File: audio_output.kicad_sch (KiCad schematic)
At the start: 33 parts, among them J8 NCJ6FA-H-0, J9 NCJ6FA-H-0, U5 OPA1656ID, U6 THAT1646, U7 THAT1646

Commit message: TVS fix
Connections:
- net AUDIO_OUT_R: now also R20.2
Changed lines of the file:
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@@
 	(wire
 		(pts
-			(xy 60.96 119.38) (xy 64.77 119.38)
-		)
-		(stroke
-			(width 0)
-			(type default)
-		)
-	)
-	(wire
-		(pts
-			(xy 99.06 166.37) (xy 99.06 168.91)
+			(xy 99.06 161.29) (xy 99.06 168.91)
 		)
 		(stroke
@@
 	(wire
 		(pts
-			(xy 81.28 191.77) (xy 81.28 179.07)
+			(xy 81.28 195.58) (xy 81.28 179.07)
 		)
 		(stroke
@@
 	(wire
 		(pts
-			(xy 135.89 166.37) (xy 135.89 168.91)
+			(xy 135.89 161.29) (xy 135.89 168.91)
 		)
 		(stroke
@@
 	(wire
 		(pts
-			(xy 99.06 189.23) (xy 99.06 191.77)
+			(xy 99.06 189.23) (xy 99.06 195.58)
 		)
 		(stroke
@@
 	(wire
 		(pts
-			(xy 118.11 191.77) (xy 118.11 179.07)
+			(xy 118.11 195.58) (xy 118.11 179.07)
 		)
 		(stroke
@@
 	(wire
 		(pts
-			(xy 135.89 189.23) (xy 135.89 191.77)
+			(xy 135.89 189.23) (xy 135.89 195.58)
 		)
 		(stroke
@@
 	(wire
 		(pts
+			(xy 59.69 119.38) (xy 64.77 119.38)
+		)
+		(stroke
+			(width 0)
+			(type default)
+		)
+	)
+	(wire
+		(pts
 			(xy 147.32 55.88) (xy 156.21 55.88)
 		)
@@
 	(symbol
 		(lib_id "power:+12VA")
-		(at 99.06 166.37 0)
+		(at 99.06 161.29 0)
 		(unit 1)
 		(exclude_from_sim no)
@@
 		(fields_autoplaced yes)
 		(property "Reference" "#PWR036"
-			(at 99.06 170.18 0)
+			(at 99.06 165.1 0)
 			(effects
 				(font
@@
 		)
 		(property "Value" "+12VA"
-			(at 99.06 161.29 0)
+			(at 99.06 156.21 0)
 			(effects
 				(font
@@
 		)
 		(property "Footprint" ""
-			(at 99.06 166.37 0)
+			(at 99.06 161.29 0)
 			(effects
 				(font
@@
 		)
 		(property "Datasheet" ""
-			(at 99.06 166.37 0)
+			(at 99.06 161.29 0)
 			(effects
 				(font
@@
 		)
 		(property "Description" "Power symbol creates a global label with name \"+12VA\""
-			(at 99.06 166.37 0)
+			(at 99.06 161.29 0)
 			(effects
 				(font
@@
 	(symbol
 		(lib_id "power:-12VA")
-		(at 99.06 191.77 180)
+		(at 99.06 195.58 180)
 		(unit 1)
 		(exclude_from_sim no)
@@
 		(fields_autoplaced yes)
 		(property "Reference" "#PWR037"
-			(at 99.06 187.96 0)
+			(at 99.06 191.77 0)
 			(effects
 				(font
@@
 		)
 		(property "Value" "-12VA"
-			(at 99.06 196.85 0)
+			(at 99.06 200.66 0)
 			(effects
 				(font
@@
 		)
 		(property "Footprint" ""
-			(at 99.06 191.77 0)
+			(at 99.06 195.58 0)
 			(effects
 				(font
@@
 		)
 		(property "Datasheet" ""
-			(at 99.06 191.77 0)
+			(at 99.06 195.58 0)
 			(effects
 				(font
@@
 		)
 		(property "Description" "Power symbol creates a global label with name \"-12VA\""
-			(at 99.06 191.77 0)
+			(at 99.06 195.58 0)
 			(effects
 				(font
@@
 	(symbol
 		(lib_id "power:-12VA")
-		(at 135.89 191.77 180)
+		(at 135.89 195.58 180)
 		(unit 1)
 		(exclude_from_sim no)
@@
 		(fields_autoplaced yes)
 		(property "Reference" "#PWR040"
-			(at 135.89 187.96 0)
+			(at 135.89 191.77 0)
 			(effects
 				(font
@@
 		)
 		(property "Value" "-12VA"
-			(at 135.89 196.85 0)
+			(at 135.89 200.66 0)
 			(effects
 				(font
@@
 		)
 		(property "Footprint" ""
-			(at 135.89 191.77 0)
+			(at 135.89 195.58 0)
 			(effects
 				(font
@@
 		)
 		(property "Datasheet" ""
-			(at 135.89 191.77 0)
+			(at 135.89 195.58 0)
 			(effects
 				(font
@@
 		)
 		(property "Description" "Power symbol creates a global label with name \"-12VA\""
-			(at 135.89 191.77 0)
+			(at 135.89 195.58 0)
 			(effects
 				(font
@@
 	(symbol
 		(lib_id "power:GND")
-		(at 81.28 191.77 0)
+		(at 81.28 195.58 0)
 		(unit 1)
 		(exclude_from_sim no)
@@
 		(fields_autoplaced yes)
 		(property "Reference" "#PWR035"
-			(at 81.28 198.12 0)
+			(at 81.28 201.93 0)
 			(effects
 				(font
@@
 		)
 		(property "Value" "GND"
-			(at 81.28 196.85 0)
+			(at 81.28 200.66 0)
 			(effects
 				(font
@@
 		)
 		(property "Footprint" ""
-			(at 81.28 191.77 0)
+			(at 81.28 195.58 0)
 			(effects
 				(font
@@
 		)
 		(property "Datasheet" ""
-			(at 81.28 191.77 0)
+			(at 81.28 195.58 0)
 			(effects
 				(font
@@
 		)
 		(property "Description" "Power symbol creates a global label with name \"GND\" , ground"
-			(at 81.28 191.77 0)
+			(at 81.28 195.58 0)
 			(effects
 				(font
@@
 	(symbol
 		(lib_id "power:+12VA")
-		(at 135.89 166.37 0)
+		(at 135.89 161.29 0)
 		(unit 1)
 		(exclude_from_sim no)
@@
 		(fields_autoplaced yes)
 		(property "Reference" "#PWR039"
-			(at 135.89 170.18 0)
+			(at 135.89 165.1 0)
 			(effects
 				(font
@@
 		)
 		(property "Value" "+12VA"
-			(at 135.89 161.29 0)
+			(at 135.89 156.21 0)
 			(effects
 				(font
@@
 		)
 		(property "Footprint" ""
-			(at 135.89 166.37 0)
+			(at 135.89 161.29 0)
 			(effects
 				(font
@@
 		)
 		(property "Datasheet" ""
-			(at 135.89 166.37 0)
+			(at 135.89 161.29 0)
 			(effects
 				(font
@@
 		)
 		(property "Description" "Power symbol creates a global label with name \"+12VA\""
-			(at 135.89 166.37 0)
+			(at 135.89 161.29 0)
 			(effects
 				(font
@@
 	(symbol
 		(lib_id "power:GND")
-		(at 118.11 191.77 0)
+		(at 118.11 195.58 0)
 		(unit 1)
 		(exclude_from_sim no)
@@
 		(fields_autoplaced yes)
 		(property "Reference" "#PWR038"
-			(at 118.11 198.12 0)
+			(at 118.11 201.93 0)
 			(effects
 				(font
@@
 		)
 		(property "Value" "GND"
-			(at 118.11 196.85 0)
+			(at 118.11 200.66 0)
 			(effects
 				(font
@@
 		)
 		(property "Footprint" ""
-			(at 118.11 191.77 0)
+			(at 118.11 195.58 0)
 			(effects
 				(font
@@
 		)
 		(property "Datasheet" ""
-			(at 118.11 191.77 0)
+			(at 118.11 195.58 0)
 			(effects
 				(font
@@
 		)
 		(property "Description" "Power symbol creates a global label with name \"GND\" , ground"
-			(at 118.11 191.77 0)
+			(at 118.11 195.58 0)
 			(effects
 				(font

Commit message: working on output
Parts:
- C16, C17: value C -> 100p C0G
- R19, R20: value R -> 2k2 1%
- R21, R22: value R -> 15k
- RV1, RV2: value R_Potentiometer_Trim -> 10k
- renumbered D8 to D10, D9 to D11, D10 to D12, D3 to D5, D4 to D6, D5 to D7, D6 to D8, D7 to D9
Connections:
- net GND: now also U5.5 (+); no longer U5.6 (-)
- net at C17.1, R20.1, R22.2: now also U5.6 (-); no longer U5.5 (+)
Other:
- moved on the sheet: C12, C13, C14, C15, U5C

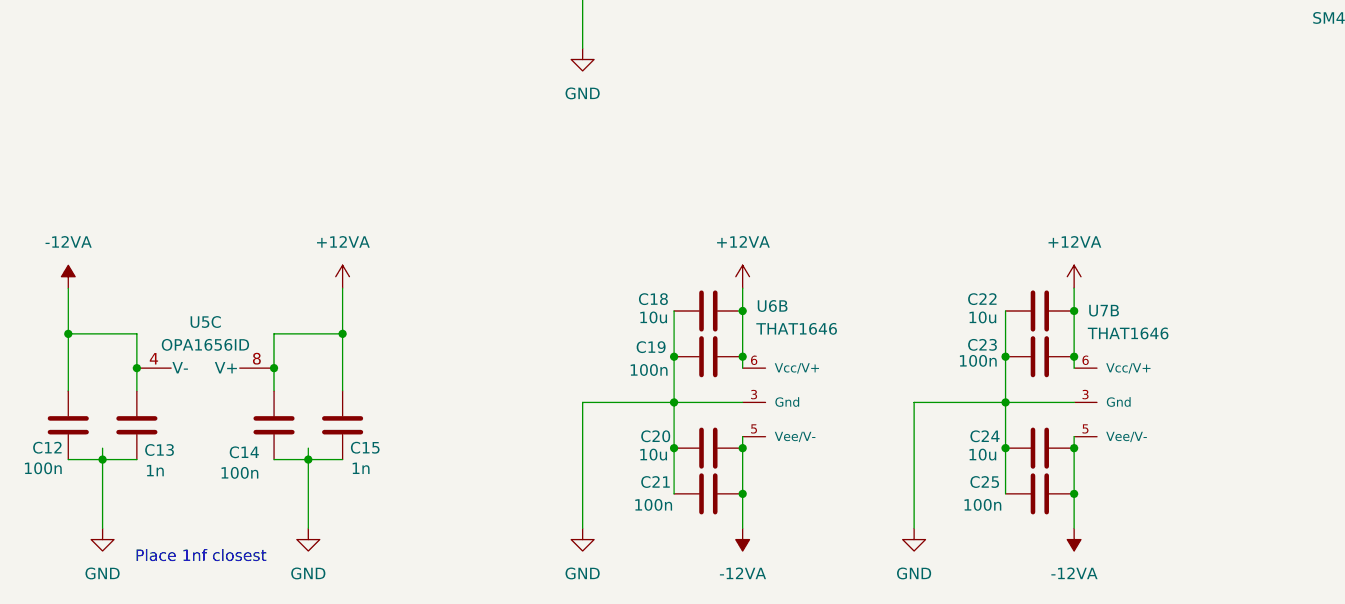
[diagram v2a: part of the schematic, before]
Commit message: fixed connectors
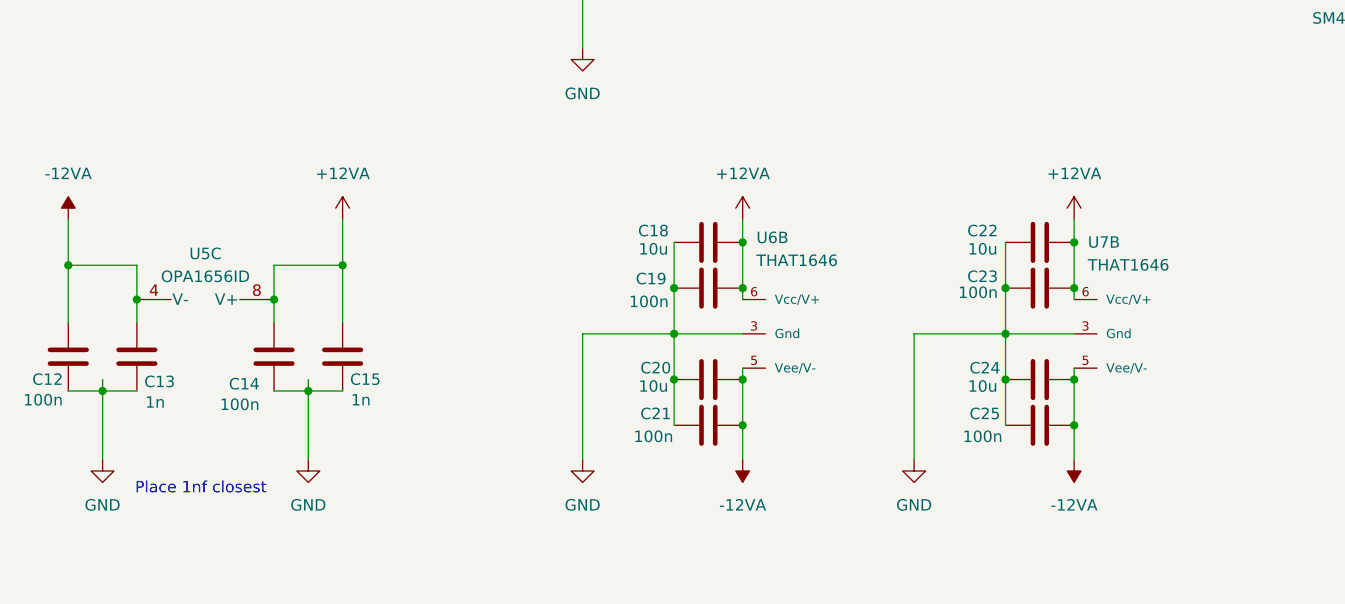
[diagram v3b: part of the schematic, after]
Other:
- moved on the sheet: C12, C13, C14, C15, C18, C19, C20, C21, C22, C23, C24, C25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

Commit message: fix seed schematic
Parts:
- renumbered J9 to J10, J8 to J9
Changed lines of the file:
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@@
 		(dnp no)
 		(fields_autoplaced yes)
-		(property "Reference" "#PWR036"
+		(property "Reference" "#PWR037"
 			(at 99.06 162.56 0)
 			(effects
@@
 			(project "daisy-studio"
 				(path "/55cca6a8-30da-4c13-b2f2-a01401e2b54c/5f2bca66-5637-48ba-a11c-0b4e3f7aa9e7"
-					(reference "#PWR036")
+					(reference "#PWR037")
 					(unit 1)
 				)
@@
 		(dnp no)
 		(fields_autoplaced yes)
-		(property "Reference" "#PWR037"
+		(property "Reference" "#PWR038"
 			(at 99.06 181.61 0)
 			(effects
@@
 			(project "daisy-studio"
 				(path "/55cca6a8-30da-4c13-b2f2-a01401e2b54c/5f2bca66-5637-48ba-a11c-0b4e3f7aa9e7"
-					(reference "#PWR037")
+					(reference "#PWR038")
 					(unit 1)
 				)
@@
 		(dnp no)
 		(fields_autoplaced yes)
-		(property "Reference" "#PWR029"
+		(property "Reference" "#PWR030"
 			(at 24.13 162.56 0)
 			(effects
@@
 			(project "daisy-studio"
 				(path "/55cca6a8-30da-4c13-b2f2-a01401e2b54c/5f2bca66-5637-48ba-a11c-0b4e3f7aa9e7"
-					(reference "#PWR029")
+					(reference "#PWR030")
 					(unit 1)
 				)
@@
 		(dnp no)
 		(fields_autoplaced yes)
-		(property "Reference" "#PWR040"
+		(property "Reference" "#PWR041"
 			(at 135.89 181.61 0)
 			(effects
@@
 			(project "daisy-studio"
 				(path "/55cca6a8-30da-4c13-b2f2-a01401e2b54c/5f2bca66-5637-48ba-a11c-0b4e3f7aa9e7"
-					(reference "#PWR040")
+					(reference "#PWR041")
 					(unit 1)
 				)
@@
 		(dnp no)
 		(fields_autoplaced yes)
-		(property "Reference" "J9"
+		(property "Reference" "J10"
 			(at 207.01 104.14 0)
 			(effects
@@
 			(project "daisy-studio"
 				(path "/55cca6a8-30da-4c13-b2f2-a01401e2b54c/5f2bca66-5637-48ba-a11c-0b4e3f7aa9e7"
-					(reference "J9")
+					(reference "J10")
 					(unit 1)
 				)
@@
 		(dnp no)
 		(fields_autoplaced yes)
-		(property "Reference" "#PWR044"
+		(property "Reference" "#PWR045"
 			(at 171.45 138.43 0)
 			(effects
@@
 			(project "daisy-studio"
 				(path "/55cca6a8-30da-4c13-b2f2-a01401e2b54c/5f2bca66-5637-48ba-a11c-0b4e3f7aa9e7"
-					(reference "#PWR044")
+					(reference "#PWR045")
 					(unit 1)
 				)
@@
 		(dnp no)
 		(fields_autoplaced yes)
-		(property "Reference" "#PWR035"
+		(property "Reference" "#PWR036"
 			(at 81.28 191.77 0)
 			(effects
@@
 			(project "daisy-studio"
 				(path "/55cca6a8-30da-4c13-b2f2-a01401e2b54c/5f2bca66-5637-48ba-a11c-0b4e3f7aa9e7"
-					(reference "#PWR035")
+					(reference "#PWR036")
 					(unit 1)
 				)
@@
 		(dnp no)
 		(fields_autoplaced yes)
-		(property "Reference" "#PWR032"
+		(property "Reference" "#PWR033"
 			(at 54.61 162.56 0)
 			(effects
@@
 			(project "daisy-studio"
 				(path "/55cca6a8-30da-4c13-b2f2-a01401e2b54c/5f2bca66-5637-48ba-a11c-0b4e3f7aa9e7"
-					(reference "#PWR032")
+					(reference "#PWR033")
 					(unit 1)
 				)
@@
 		(on_board yes)
 		(dnp no)
-		(property "Reference" "#PWR043"
+		(property "Reference" "#PWR044"
 			(at 171.45 101.6 0)
 			(effects
@@
 			(project "daisy-studio"
 				(path "/55cca6a8-30da-4c13-b2f2-a01401e2b54c/5f2bca66-5637-48ba-a11c-0b4e3f7aa9e7"
-					(reference "#PWR043")
+					(reference "#PWR044")
 					(unit 1)
 				)
@@
 		(on_board yes)
 		(dnp no)
-		(property "Reference" "#PWR041"
+		(property "Reference" "#PWR042"
 			(at 171.45 35.56 0)
 			(effects
@@
 			(project "daisy-studio"
 				(path "/55cca6a8-30da-4c13-b2f2-a01401e2b54c/5f2bca66-5637-48ba-a11c-0b4e3f7aa9e7"
-					(reference "#PWR041")
+					(reference "#PWR042")
 					(unit 1)
 				)
@@
 		(on_board yes)
 		(dnp no)
-		(property "Reference" "#PWR030"
+		(property "Reference" "#PWR031"
 			(at 27.94 191.77 0)
 			(effects
@@
 			(project "daisy-studio"
 				(path "/55cca6a8-30da-4c13-b2f2-a01401e2b54c/5f2bca66-5637-48ba-a11c-0b4e3f7aa9e7"
-					(reference "#PWR030")
+					(reference "#PWR031")
 					(unit 1)
 				)
@@
 		(on_board yes)
 		(dnp no)
-		(property "Reference" "#PWR033"
+		(property "Reference" "#PWR034"
 			(at 81.28 80.01 0)
 			(effects
@@
 			(project "daisy-studio"
 				(path "/55cca6a8-30da-4c13-b2f2-a01401e2b54c/5f2bca66-5637-48ba-a11c-0b4e3f7aa9e7"
-					(reference "#PWR033")
+					(reference "#PWR034")
 					(unit 1)
 				)
@@
 		(on_board yes)
 		(dnp no)
-		(property "Reference" "#PWR031"
+		(property "Reference" "#PWR032"
 			(at 50.8 191.77 0)
 			(effects
@@
 			(project "daisy-studio"
 				(path "/55cca6a8-30da-4c13-b2f2-a01401e2b54c/5f2bca66-5637-48ba-a11c-0b4e3f7aa9e7"
-					(reference "#PWR031")
+					(reference "#PWR032")
 					(unit 1)
 				)
@@
 		(on_board yes)
 		(dnp no)
-		(property "Reference" "#PWR045"
+		(property "Reference" "#PWR046"
 			(at 198.12 82.55 0)
 			(effects
@@
 			(project "daisy-studio"
 				(path "/55cca6a8-30da-4c13-b2f2-a01401e2b54c/5f2bca66-5637-48ba-a11c-0b4e3f7aa9e7"
-					(reference "#PWR045")
+					(reference "#PWR046")
 					(unit 1)
 				)
@@
 		(dnp no)
 		(fields_autoplaced yes)
-		(property "Reference" "J8"
+		(property "Reference" "J9"
 			(at 214.63 71.7549 0)
 			(effects
@@
 			(project "daisy-studio"
 				(path "/55cca6a8-30da-4c13-b2f2-a01401e2b54c/5f2bca66-5637-48ba-a11c-0b4e3f7aa9e7"
-					(reference "J8")
+					(reference "J9")
 					(unit 2)
 				)
@@
 		(dnp no)
 		(fields_autoplaced yes)
-		(property "Reference" "#PWR039"
+		(property "Reference" "#PWR040"
 			(at 135.89 162.56 0)
 			(effects
@@
 			(project "daisy-studio"
 				(path "/55cca6a8-30da-4c13-b2f2-a01401e2b54c/5f2bca66-5637-48ba-a11c-0b4e3f7aa9e7"
-					(reference "#PWR039")
+					(reference "#PWR040")
 					(unit 1)
 				)
@@
 		(dnp no)
 		(fields_autoplaced yes)
-		(property "Reference" "#PWR034"
+		(property "Reference" "#PWR035"
 			(at 81.28 146.05 0)
 			(effects
@@
 			(project "daisy-studio"
 				(path "/55cca6a8-30da-4c13-b2f2-a01401e2b54c/5f2bca66-5637-48ba-a11c-0b4e3f7aa9e7"
-					(reference "#PWR034")
+					(reference "#PWR035")
 					(unit 1)
 				)
@@
 		(on_board yes)
 		(dnp no)
-		(property "Reference" "#PWR046"
+		(property "Reference" "#PWR047"
 			(at 198.12 148.59 0)
 			(effects
@@
 			(project "daisy-studio"
 				(path "/55cca6a8-30da-4c13-b2f2-a01401e2b54c/5f2bca66-5637-48ba-a11c-0b4e3f7aa9e7"
-					(reference "#PWR046")
+					(reference "#PWR047")
 					(unit 1)
 				)
@@
 		(dnp no)
 		(fields_autoplaced yes)
-		(property "Reference" "#PWR038"
+		(property "Reference" "#PWR039"
 			(at 118.11 191.77 0)
 			(effects
@@
 			(project "daisy-studio"
 				(path "/55cca6a8-30da-4c13-b2f2-a01401e2b54c/5f2bca66-5637-48ba-a11c-0b4e3f7aa9e7"
-					(reference "#PWR038")
+					(reference "#PWR039")
 					(unit 1)
 				)
@@
 		(dnp no)
 		(fields_autoplaced yes)
-		(property "Reference" "J8"
+		(property "Reference" "J9"
 			(at 207.01 38.1 0)
 			(effects
@@
 			(project "daisy-studio"
 				(path "/55cca6a8-30da-4c13-b2f2-a01401e2b54c/5f2bca66-5637-48ba-a11c-0b4e3f7aa9e7"
-					(reference "J8")
+					(reference "J9")
 					(unit 1)
 				)
@@
 		(dnp no)
 		(fields_autoplaced yes)
-		(property "Reference" "#PWR042"
+		(property "Reference" "#PWR043"
 			(at 171.45 72.39 0)
 			(effects
@@
 			(project "daisy-studio"
 				(path "/55cca6a8-30da-4c13-b2f2-a01401e2b54c/5f2bca66-5637-48ba-a11c-0b4e3f7aa9e7"
-					(reference "#PWR042")
+					(reference "#PWR043")
 					(unit 1)
 				)
@@
 		(dnp no)
 		(fields_autoplaced yes)
-		(property "Reference" "J9"
+		(property "Reference" "J10"
 			(at 214.63 137.7949 0)
 			(effects
@@
 			(project "daisy-studio"
 				(path "/55cca6a8-30da-4c13-b2f2-a01401e2b54c/5f2bca66-5637-48ba-a11c-0b4e3f7aa9e7"
-					(reference "J9")
+					(reference "J10")
 					(unit 2)
 				)

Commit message: footprints fixed
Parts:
- RV1, RV2: footprint (none) -> Potentiometer_THT:Potentiometer_Bourns_3296W_Vertical
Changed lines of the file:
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@@
 			)
 		)
-		(property "Footprint" ""
+		(property "Footprint" "Potentiometer_THT:Potentiometer_Bourns_3296W_Vertical"
 			(at 107.95 35.56 0)
 			(effects
@@
 			)
 		)
-		(property "Footprint" ""
+		(property "Footprint" "Potentiometer_THT:Potentiometer_Bourns_3296W_Vertical"
 			(at 107.95 101.6 0)
 			(effects

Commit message: update power - still not happy
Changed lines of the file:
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@@
-	(wire
-		(pts
-			(xy 50.8 177.8) (xy 50.8 176.53)
-		)
-		(stroke
-			(width 0)
-			(type default)
-		)
-	)
 	(wire
 		(pts
@@
 		)
 		(stroke
-			(width 0)
-			(type default)
-		)
-	)
-	(wire
-		(pts
-			(xy 27.94 177.8) (xy 27.94 176.53)
-		)
-		(stroke
